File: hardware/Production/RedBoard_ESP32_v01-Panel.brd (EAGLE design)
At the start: 246.1 x 248.9 mm, 2454 parts, among them J1 5.5x2.1mm Barrel, J101 USB C, J102 USB_SOLDER_PADS, J103 M10NO_SILK, J108 QWIIC_RIGHT_ANGLE, J109 MICRO-SD-PUSH-PUSH-EXT-PIN, J110 5.5x2.1mm Barrel, J117 USB C, J118 USB_SOLDER_PADS, J119 M10NO_SILK, J124 QWIIC_RIGHT_ANGLE, J125 MICRO-SD-PUSH-PUSH-EXT-PIN, J126 5.5x2.1mm Barrel, J13 QWIIC_RIGHT_ANGLE, J133 USB C, J134 USB_SOLDER_PADS, J135 M10NO_SILK, J140 QWIIC_RIGHT_ANGLE, J141 MICRO-SD-PUSH-PUSH-EXT-PIN, J142 5.5x2.1mm Barrel, J149 USB C, J15 MICRO-SD-PUSH-PUSH-EXT-PIN, J150 USB_SOLDER_PADS, J151 M10NO_SILK, J156 QWIIC_RIGHT_ANGLE, J157 MICRO-SD-PUSH-PUSH-EXT-PIN, J158 5.5x2.1mm Barrel, J165 USB C, J166 USB_SOLDER_PADS, J167 M10NO_SILK, J172 QWIIC_RIGHT_ANGLE, J173 MICRO-SD-PUSH-PUSH-EXT-PIN, J174 5.5x2.1mm Barrel, J181 USB C, J182 USB_SOLDER_PADS, J183 M10NO_SILK, J188 QWIIC_RIGHT_ANGLE, J189 MICRO-SD-PUSH-PUSH-EXT-PIN, J190 5.5x2.1mm Barrel, J2 USB C, J21 USB C, J22 USB_SOLDER_PADS, J23 M10NO_SILK, J28 QWIIC_RIGHT_ANGLE, J29 MICRO-SD-PUSH-PUSH-EXT-PIN, J3 USB_SOLDER_PADS, J30 5.5x2.1mm Barrel, J37 USB C, J38 USB_SOLDER_PADS, J39 M10NO_SILK, J44 QWIIC_RIGHT_ANGLE, J45 MICRO-SD-PUSH-PUSH-EXT-PIN, J46 5.5x2.1mm Barrel, J5 M10NO_SILK, J53 USB C, J54 USB_SOLDER_PADS, J55 M10NO_SILK, J60 QWIIC_RIGHT_ANGLE, J61 MICRO-SD-PUSH-PUSH-EXT-PIN, J62 5.5x2.1mm Barrel, J69 USB C, J70 USB_SOLDER_PADS, J71 M10NO_SILK, J76 QWIIC_RIGHT_ANGLE, J77 MICRO-SD-PUSH-PUSH-EXT-PIN, J78 5.5x2.1mm Barrel, J85 USB C, J86 USB_SOLDER_PADS, J87 M10NO_SILK, J92 QWIIC_RIGHT_ANGLE, J93 MICRO-SD-PUSH-PUSH-EXT-PIN, J94 5.5x2.1mm Barrel, Q1 MBT3904DW1T1, Q100 20V/4.2A/52mΩ/1.4W, Q102 20V/4.2A/52mΩ/1.4W, Q104 20V/4.2A/52mΩ/1.4W, Q105 MBT3904DW1T1, Q107 20V/4.2A/52mΩ/1.4W, Q109 20V/4.2A/52mΩ/1.4W, Q11 20V/4.2A/52mΩ/1.4W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

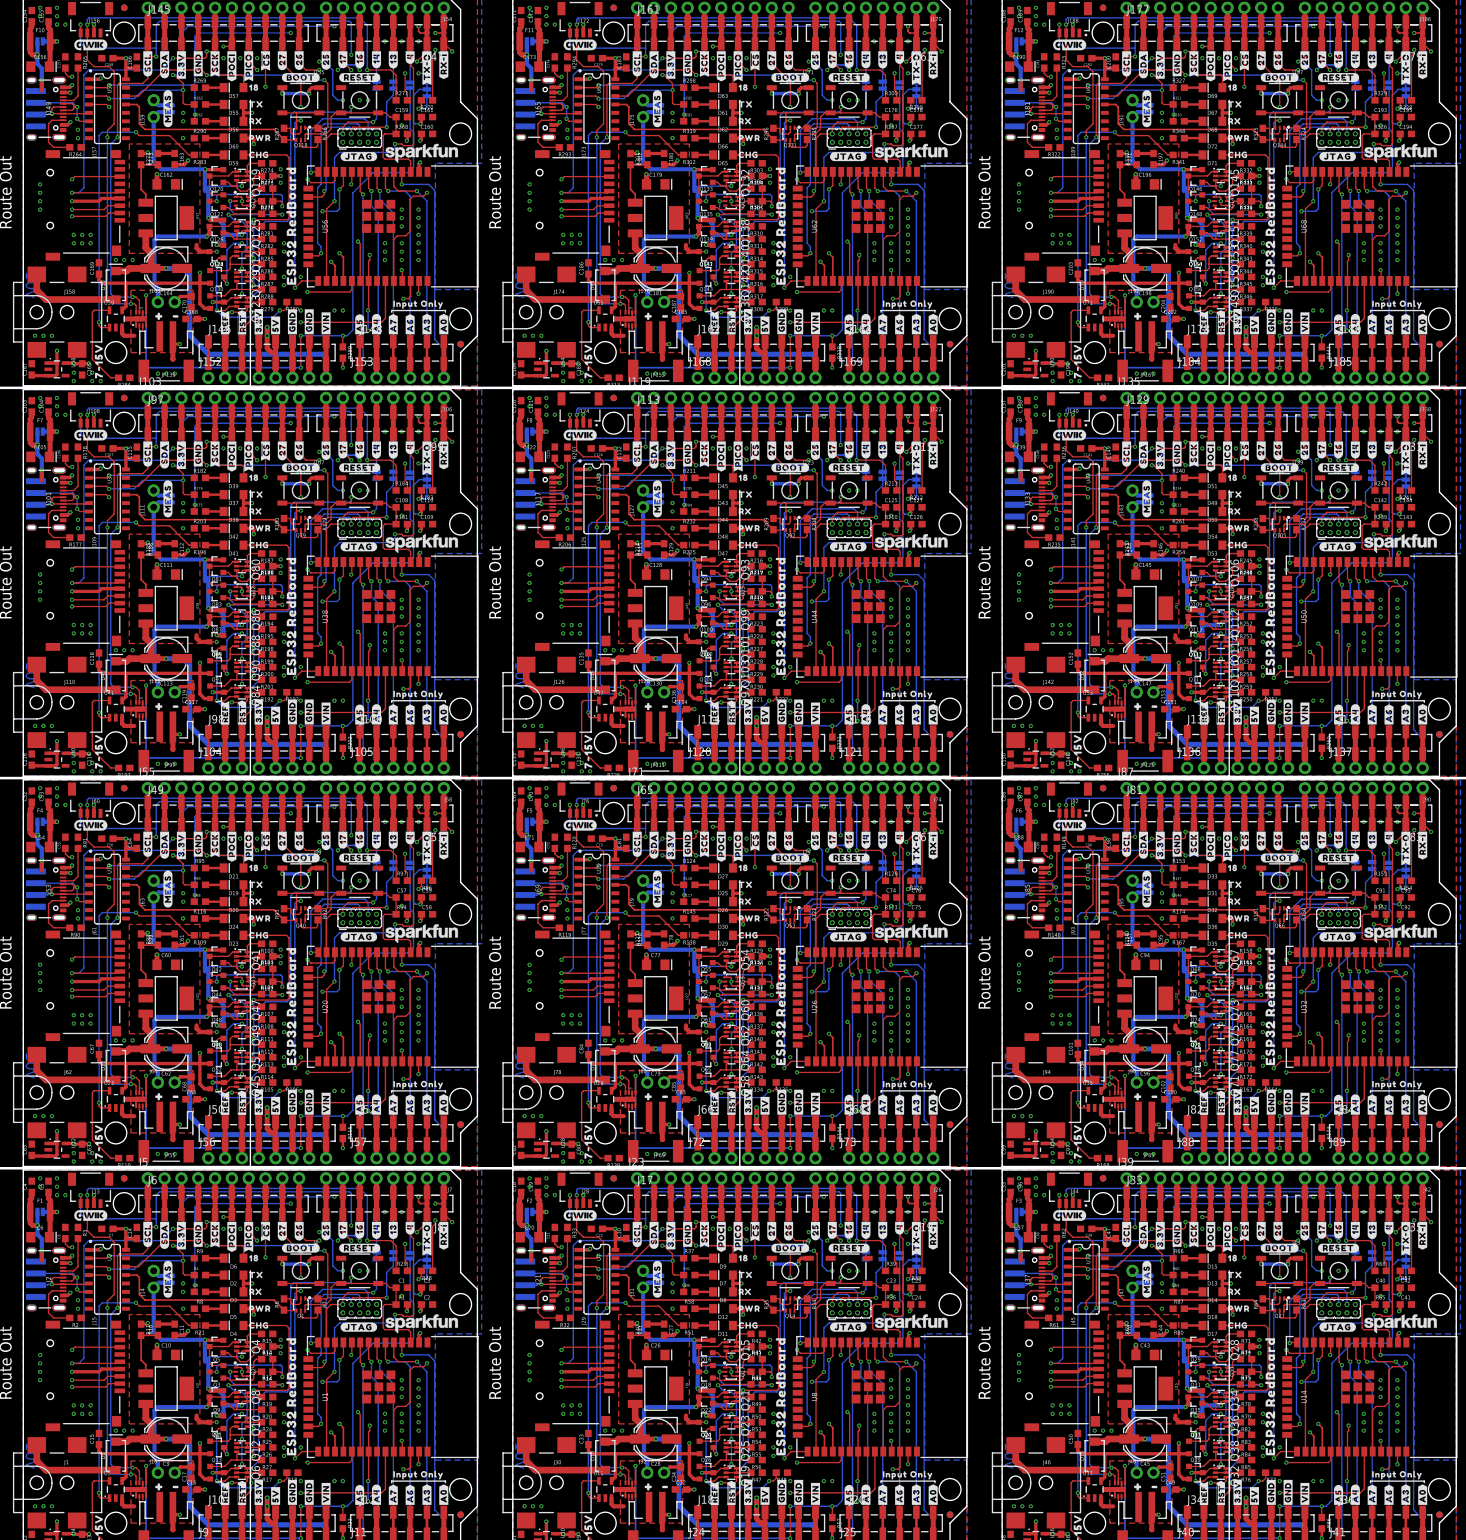
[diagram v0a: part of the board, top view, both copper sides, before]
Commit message: Added Test Point per Eric Orosel request.
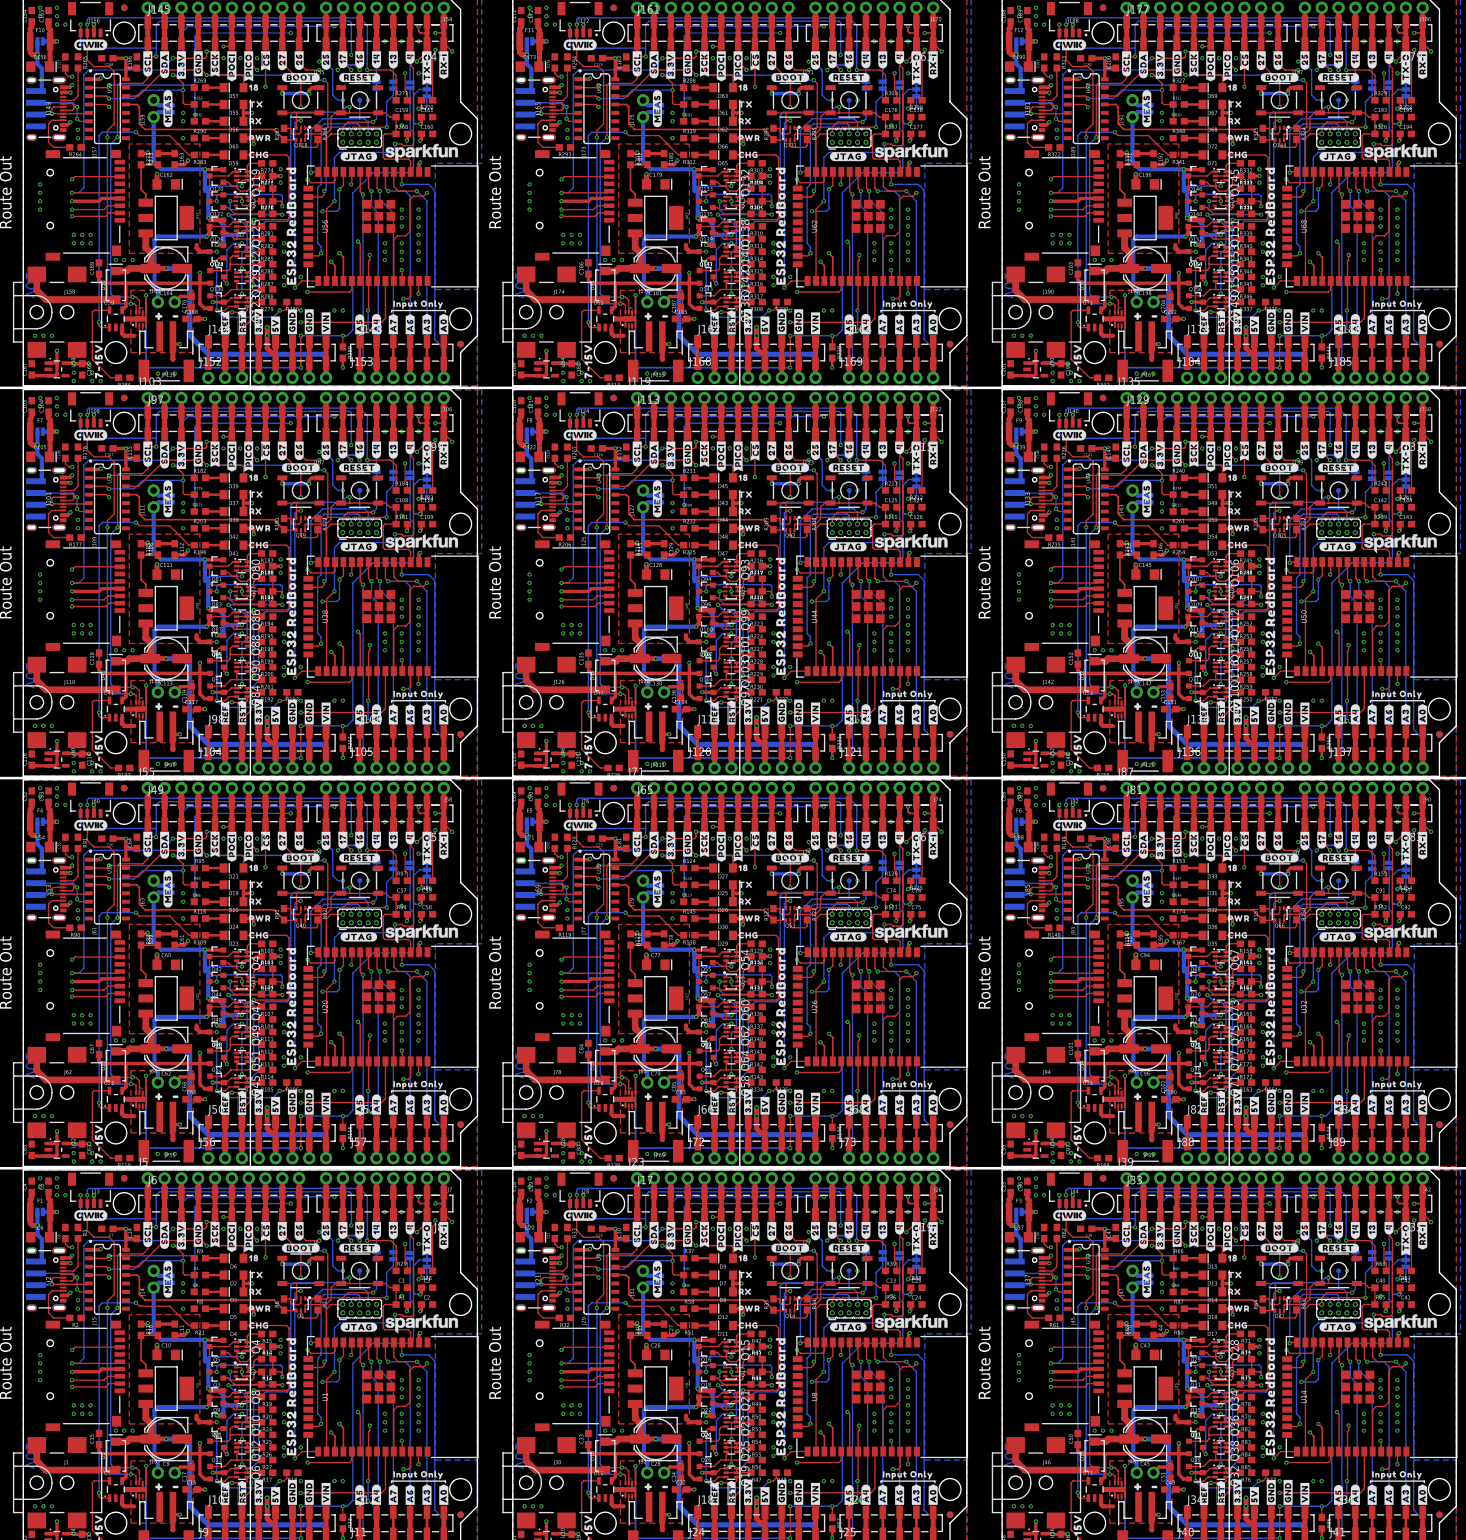
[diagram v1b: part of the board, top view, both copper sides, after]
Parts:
- added TP1, TP10, TP11, TP12, TP2, TP3, TP4, TP5, TP6, TP7, TP8, TP9: TEST-POINT3, SparkFun-Connectors:PAD.03X.03
- added U$1129: (no value), output-ESP32:#1850
- added U$1130: (no value), output-ESP32:#I2C#1855
- added U$1131: (no value), output-ESP32:##ALERT##1852
- added U$1132: (no value), output-ESP32:#TMS#1854
- added U$1133: (no value), output-ESP32:#TCK#1853
- added U$1134: (no value), output-ESP32:MADE_IN_THE_USA321857
- added U$1135: (no value), output-ESP32:ESP32_REDBOARD321857
- added U$1136: (no value), output-ESP32:REDBOARD321856
- added U$1137, U$1138: (no value), output-ESP32:INPUT_ONLY321867
- added U$1139: (no value), output-ESP32:##ALERT##4#321866
- added U$1140: (no value), output-ESP32:TP1321868
- U$100: device output-ESP32:#SCK#31 -> output-ESP32:#GND#32
- U$1000: device output-ESP32:#IOREF#321865 -> output-ESP32:#34#A6#32321865
- U$1001: device output-ESP32:#3#RX#I#32321869 -> output-ESP32:#35#A7#321862
- U$1002: device output-ESP32:#1#TX#O#32321869 -> output-ESP32:#32#A4#32321865
- U$1003: device output-ESP32:#13#TCK#32321869 -> output-ESP32:#34#A6#321862
- U$1004: device output-ESP32:#14#TMS#32321869 -> output-ESP32:#VIN#321862
- U$1005, U$723: device output-ESP32:#16#32321869 -> output-ESP32:#GND#321863
- U$1006: device output-ESP32:#17#32321869 -> output-ESP32:#5V#321864
- U$1007: device output-ESP32:#25#32321869 -> output-ESP32:#3#3V#321864
- U$1008: device output-ESP32:#26#32321869 -> output-ESP32:#GND#321863
- U$1009: device output-ESP32:#5##CS##32321869 -> output-ESP32:##RESET##321864
- U$101: device output-ESP32:#POCI#30 -> output-ESP32:#SCK#31
- U$1010: device output-ESP32:#23#PICO#321866 -> output-ESP32:#IOREF#321865
- U$1011: device output-ESP32:#19#POCI#321866 -> output-ESP32:#3#RX#I#32321869
- U$1012: device output-ESP32:#18#SCK#32321869 -> output-ESP32:#1#TX#O#32321869
- U$1013: device output-ESP32:#21#SDA#32321869 -> output-ESP32:#13#TCK#32321869
- U$1014: device output-ESP32:#22#SCL#32321869 -> output-ESP32:#14#TMS#32321869
- U$1015: device output-ESP32:#27#32321869 -> output-ESP32:#16#32321869
- U$1016: device output-ESP32:#GND#321866 -> output-ESP32:#17#32321869
- U$1017: device output-ESP32:#3#3V#321866 -> output-ESP32:#25#32321869
- U$1018: device output-ESP32:#MEAS#1851 -> output-ESP32:#26#32321869
- U$1019: device output-ESP32:#BYP#35 -> output-ESP32:#5##CS##32321869
- U$102: device output-ESP32:#PICO#29 -> output-ESP32:#POCI#30
- U$1020: device output-ESP32:D#32321863 -> output-ESP32:#23#PICO#321866
- U$1021: device output-ESP32:D#32321862 -> output-ESP32:#19#POCI#321866
- U$1022: device output-ESP32:G32321864 -> output-ESP32:#18#SCK#32321869
- U$1023: device output-ESP32:#1849 -> output-ESP32:#21#SDA#32321869
- U$1024: device output-ESP32:#1850 -> output-ESP32:#22#SCL#32321869
- U$1025: device output-ESP32:#I2C#1855 -> output-ESP32:#27#32321869
- U$1026: device output-ESP32:##ALERT##1852 -> output-ESP32:#GND#321866
- U$1027: device output-ESP32:#TMS#1854 -> output-ESP32:#3#3V#321866
- U$1028: device output-ESP32:#TCK#1853 -> output-ESP32:#MEAS#1851
- U$1029: device output-ESP32:MADE_IN_THE_USA321857 -> output-ESP32:#BYP#35
- U$103: device output-ESP32:1836 -> output-ESP32:#PICO#29
- U$1030: device output-ESP32:ESP32_REDBOARD321857 -> output-ESP32:D#32321863
- U$1031: device output-ESP32:REDBOARD321856 -> output-ESP32:D#32321862
- U$1032, U$1127: device output-ESP32:INPUT_ONLY321867 -> output-ESP32:G32321864
- U$1033, U$938: device output-ESP32:INPUT_ONLY321867 -> output-ESP32:#1849
- U$1034: device output-ESP32:##ALERT##4#321866 -> output-ESP32:#1850
- U$1035: device output-ESP32:V323252 -> output-ESP32:#I2C#1855
- U$1036: device output-ESP32:#SCL#34 -> output-ESP32:##ALERT##1852
- U$1037: device output-ESP32:#SDA#33 -> output-ESP32:#TMS#1854
- U$1038: device output-ESP32:#3#3V#33 -> output-ESP32:#TCK#1853
- U$1039: device output-ESP32:#GND#32 -> output-ESP32:MADE_IN_THE_USA321857
- U$104: device output-ESP32:##CS##28 -> output-ESP32:1836
- U$1040: device output-ESP32:#SCK#31 -> output-ESP32:ESP32_REDBOARD321857
- U$1041: device output-ESP32:#POCI#30 -> output-ESP32:REDBOARD321856
- U$1042, U$948: device output-ESP32:#PICO#29 -> output-ESP32:INPUT_ONLY321867
- U$1043: device output-ESP32:1836 -> output-ESP32:INPUT_ONLY321867
- U$1044: device output-ESP32:##CS##28 -> output-ESP32:##ALERT##4#321866
- U$1045: device output-ESP32:#27#27 -> output-ESP32:TP1321868
- U$1046: device output-ESP32:#26#26 -> output-ESP32:V323252
- U$1047: device output-ESP32:TX1838 -> output-ESP32:#SCL#34
- U$1048: device output-ESP32:RX1839 -> output-ESP32:#SDA#33
- U$1049: device output-ESP32:PWR1837 -> output-ESP32:#3#3V#33
- U$105: device output-ESP32:#27#27 -> output-ESP32:##CS##28
- U$1050: device output-ESP32:CHG1840 -> output-ESP32:#GND#32
- U$1051: device output-ESP32:#25#18 -> output-ESP32:#SCK#31
- U$1052: device output-ESP32:#17#17 -> output-ESP32:#POCI#30
- U$1053: device output-ESP32:#16#15 -> output-ESP32:#PICO#29
- U$1054: device output-ESP32:#14#14 -> output-ESP32:1836
- U$1055: device output-ESP32:#13#5 -> output-ESP32:##CS##28
- U$1056: device output-ESP32:#4#2 -> output-ESP32:#27#27
- U$1057: device output-ESP32:#TX#O#0 -> output-ESP32:#26#26
- U$1058: device output-ESP32:#RX#I#1 -> output-ESP32:TX1838
- U$1059: device output-ESP32:#RESET#1842 -> output-ESP32:RX1839
- U$106: device output-ESP32:#26#26 -> output-ESP32:#27#27
- U$1060: device output-ESP32:#BOOT#1841 -> output-ESP32:PWR1837
- U$1061: device output-ESP32:#JTAG#1847 -> output-ESP32:CHG1840
- U$1062: device output-ESP32:#A0#1843 -> output-ESP32:#25#18
- U$1063: device output-ESP32:#A3#1843 -> output-ESP32:#17#17
- U$1064: device output-ESP32:#A6#1843 -> output-ESP32:#16#15
- U$1065: device output-ESP32:#A7#1843 -> output-ESP32:#14#14
- U$1066: device output-ESP32:#A4#1843 -> output-ESP32:#13#5
- U$1067: device output-ESP32:#A5#1843 -> output-ESP32:#4#2
- U$1068: device output-ESP32:#VIN#1843 -> output-ESP32:#TX#O#0
- U$1069: device output-ESP32:#GND#1844 -> output-ESP32:#RX#I#1
- U$107: device output-ESP32:TX1838 -> output-ESP32:#26#26
- U$1070, U$975: device output-ESP32:#GND#1844 -> output-ESP32:#RESET#1842
- U$1071: device output-ESP32:#5V#1845 -> output-ESP32:#BOOT#1841
- U$1072: device output-ESP32:#3#3V#1845 -> output-ESP32:#JTAG#1847
- U$1073: device output-ESP32:##RST##1845 -> output-ESP32:#A0#1843
- U$1074: device output-ESP32:#REF#1846 -> output-ESP32:#A3#1843
- U$1075: device output-ESP32:#MEAS#1851 -> output-ESP32:#A6#1843
- U$1076: device output-ESP32:#1849 -> output-ESP32:#A7#1843
- U$1077: device output-ESP32:#1850 -> output-ESP32:#A4#1843
- U$1078: device output-ESP32:#BATT#1848 -> output-ESP32:#A5#1843
- U$1079: device output-ESP32:#JTAG#1847 -> output-ESP32:#VIN#1843
- U$108: device output-ESP32:RX1839 -> output-ESP32:TX1838
- U$1080, U$986: device output-ESP32:ESP321855 -> output-ESP32:#GND#1844
- U$1081: device output-ESP32:7#15V32321861 -> output-ESP32:#GND#1844
- U$1082: device output-ESP32:#39#A3#321862 -> output-ESP32:#5V#1845
- U$1083: device output-ESP32:#36#A0#321862 -> output-ESP32:#3#3V#1845
- U$1084: device output-ESP32:#34#A6#32321865 -> output-ESP32:##RST##1845
- U$1085: device output-ESP32:#35#A7#321862 -> output-ESP32:#REF#1846
- U$1086: device output-ESP32:#32#A4#32321865 -> output-ESP32:#MEAS#1851
- U$1087: device output-ESP32:#34#A6#321862 -> output-ESP32:#1849
- U$1088: device output-ESP32:#VIN#321862 -> output-ESP32:#1850
- U$1089: device output-ESP32:#GND#321863 -> output-ESP32:#BATT#1848
- U$109: device output-ESP32:PWR1837 -> output-ESP32:RX1839
- U$1090: device output-ESP32:#5V#321864 -> output-ESP32:#JTAG#1847
- U$1091: device output-ESP32:#3#3V#321864 -> output-ESP32:ESP321855
- U$1092, U$807: device output-ESP32:#GND#321863 -> output-ESP32:7#15V32321861
- U$1093: device output-ESP32:##RESET##321864 -> output-ESP32:#39#A3#321862
- U$1094: device output-ESP32:#IOREF#321865 -> output-ESP32:#36#A0#321862
- U$1095: device output-ESP32:#3#RX#I#32321869 -> output-ESP32:#34#A6#32321865
- U$1096: device output-ESP32:#1#TX#O#32321869 -> output-ESP32:#35#A7#321862
- U$1097: device output-ESP32:#13#TCK#32321869 -> output-ESP32:#32#A4#32321865
- U$1098: device output-ESP32:#14#TMS#32321869 -> output-ESP32:#34#A6#321862
- U$1099: device output-ESP32:#16#32321869 -> output-ESP32:#VIN#321862
- U$110: device output-ESP32:CHG1840 -> output-ESP32:PWR1837
- U$1100, U$818: device output-ESP32:#17#32321869 -> output-ESP32:#GND#321863
- U$1101: device output-ESP32:#25#32321869 -> output-ESP32:#5V#321864
- U$1102: device output-ESP32:#26#32321869 -> output-ESP32:#3#3V#321864
- U$1103: device output-ESP32:#5##CS##32321869 -> output-ESP32:#GND#321863
- U$1104: device output-ESP32:#23#PICO#321866 -> output-ESP32:##RESET##321864
- U$1105: device output-ESP32:#19#POCI#321866 -> output-ESP32:#IOREF#321865
- U$1106: device output-ESP32:#18#SCK#32321869 -> output-ESP32:#3#RX#I#32321869
- U$1107: device output-ESP32:#21#SDA#32321869 -> output-ESP32:#1#TX#O#32321869
- U$1108: device output-ESP32:#22#SCL#32321869 -> output-ESP32:#13#TCK#32321869
- U$1109: device output-ESP32:#27#32321869 -> output-ESP32:#14#TMS#32321869
- U$111: device output-ESP32:#25#18 -> output-ESP32:CHG1840
- U$1110: device output-ESP32:#GND#321866 -> output-ESP32:#16#32321869
- U$1111: device output-ESP32:#3#3V#321866 -> output-ESP32:#17#32321869
- U$1112: device output-ESP32:#MEAS#1851 -> output-ESP32:#25#32321869
- U$1113: device output-ESP32:#BYP#35 -> output-ESP32:#26#32321869
- U$1114: device output-ESP32:D#32321863 -> output-ESP32:#5##CS##32321869
- U$1115: device output-ESP32:D#32321862 -> output-ESP32:#23#PICO#321866
- U$1116: device output-ESP32:G32321864 -> output-ESP32:#19#POCI#321866
- U$1117: device output-ESP32:#1849 -> output-ESP32:#18#SCK#32321869
- U$1118: device output-ESP32:#1850 -> output-ESP32:#21#SDA#32321869
- U$1119: device output-ESP32:#I2C#1855 -> output-ESP32:#22#SCL#32321869
- U$112: device output-ESP32:#17#17 -> output-ESP32:#25#18
- U$1120: device output-ESP32:##ALERT##1852 -> output-ESP32:#27#32321869
- U$1121: device output-ESP32:#TMS#1854 -> output-ESP32:#GND#321866
- U$1122: device output-ESP32:#TCK#1853 -> output-ESP32:#3#3V#321866
- U$1123: device output-ESP32:MADE_IN_THE_USA321857 -> output-ESP32:#MEAS#1851
- U$1124: device output-ESP32:ESP32_REDBOARD321857 -> output-ESP32:#BYP#35
- U$1125: device output-ESP32:REDBOARD321856 -> output-ESP32:D#32321863
- U$1126: device output-ESP32:INPUT_ONLY321867 -> output-ESP32:D#32321862
- U$1128: device output-ESP32:##ALERT##4#321866 -> output-ESP32:#1849
- U$113: device output-ESP32:#16#15 -> output-ESP32:#17#17
- U$114: device output-ESP32:#14#14 -> output-ESP32:#16#15
- U$115: device output-ESP32:#13#5 -> output-ESP32:#14#14
- U$116: device output-ESP32:#4#2 -> output-ESP32:#13#5
- U$117: device output-ESP32:#TX#O#0 -> output-ESP32:#4#2
- U$118: device output-ESP32:#RX#I#1 -> output-ESP32:#TX#O#0
- U$119: device output-ESP32:#RESET#1842 -> output-ESP32:#RX#I#1
- U$120: device output-ESP32:#BOOT#1841 -> output-ESP32:#RESET#1842
- U$121: device output-ESP32:#JTAG#1847 -> output-ESP32:#BOOT#1841
- U$122: device output-ESP32:#A0#1843 -> output-ESP32:#JTAG#1847
- U$123: device output-ESP32:#A3#1843 -> output-ESP32:#A0#1843
- U$124: device output-ESP32:#A6#1843 -> output-ESP32:#A3#1843
- U$125: device output-ESP32:#A7#1843 -> output-ESP32:#A6#1843
- U$126: device output-ESP32:#A4#1843 -> output-ESP32:#A7#1843
- U$127: device output-ESP32:#A5#1843 -> output-ESP32:#A4#1843
- U$128: device output-ESP32:#VIN#1843 -> output-ESP32:#A5#1843
- U$129, U$224: device output-ESP32:#GND#1844 -> output-ESP32:#VIN#1843
- U$131, U$225: device output-ESP32:#5V#1845 -> output-ESP32:#GND#1844
- U$132: device output-ESP32:#3#3V#1845 -> output-ESP32:#5V#1845
- U$133: device output-ESP32:##RST##1845 -> output-ESP32:#3#3V#1845
- U$134: device output-ESP32:#REF#1846 -> output-ESP32:##RST##1845
- U$135: device output-ESP32:#MEAS#1851 -> output-ESP32:#REF#1846
- U$136, U$553: device output-ESP32:#1849 -> output-ESP32:#MEAS#1851
- U$137, U$178: device output-ESP32:#1850 -> output-ESP32:#1849
- U$138: device output-ESP32:#BATT#1848 -> output-ESP32:#1850
- U$139: device output-ESP32:#JTAG#1847 -> output-ESP32:#BATT#1848
- U$140: device output-ESP32:ESP321855 -> output-ESP32:#JTAG#1847
- U$141: device output-ESP32:7#15V32321861 -> output-ESP32:ESP321855
- U$142: device output-ESP32:#39#A3#321862 -> output-ESP32:7#15V32321861
- U$143: device output-ESP32:#36#A0#321862 -> output-ESP32:#39#A3#321862
- U$144: device output-ESP32:#34#A6#32321865 -> output-ESP32:#36#A0#321862
- U$145: device output-ESP32:#35#A7#321862 -> output-ESP32:#34#A6#32321865
- U$146: device output-ESP32:#32#A4#32321865 -> output-ESP32:#35#A7#321862
- U$147: device output-ESP32:#34#A6#321862 -> output-ESP32:#32#A4#32321865
- U$148: device output-ESP32:#VIN#321862 -> output-ESP32:#34#A6#321862
- U$149, U$434: device output-ESP32:#GND#321863 -> output-ESP32:#VIN#321862
- U$150: device output-ESP32:#5V#321864 -> output-ESP32:#GND#321863
- U$151: device output-ESP32:#3#3V#321864 -> output-ESP32:#5V#321864
- U$152: device output-ESP32:#GND#321863 -> output-ESP32:#3#3V#321864
- U$153, U$435: device output-ESP32:##RESET##321864 -> output-ESP32:#GND#321863
- U$154: device output-ESP32:#IOREF#321865 -> output-ESP32:##RESET##321864
- U$155: device output-ESP32:#3#RX#I#32321869 -> output-ESP32:#IOREF#321865
- U$156: device output-ESP32:#1#TX#O#32321869 -> output-ESP32:#3#RX#I#32321869
- U$157: device output-ESP32:#13#TCK#32321869 -> output-ESP32:#1#TX#O#32321869
- U$158: device output-ESP32:#14#TMS#32321869 -> output-ESP32:#13#TCK#32321869
- U$159: device output-ESP32:#16#32321869 -> output-ESP32:#14#TMS#32321869
- U$160: device output-ESP32:#17#32321869 -> output-ESP32:#16#32321869
- U$161: device output-ESP32:#25#32321869 -> output-ESP32:#17#32321869
- U$162: device output-ESP32:#26#32321869 -> output-ESP32:#25#32321869
- U$163: device output-ESP32:#5##CS##32321869 -> output-ESP32:#26#32321869
- U$164: device output-ESP32:#23#PICO#321866 -> output-ESP32:#5##CS##32321869
- U$165: device output-ESP32:#19#POCI#321866 -> output-ESP32:#23#PICO#321866
- U$166: device output-ESP32:#18#SCK#32321869 -> output-ESP32:#19#POCI#321866
- U$167: device output-ESP32:#21#SDA#32321869 -> output-ESP32:#18#SCK#32321869
- U$168: device output-ESP32:#22#SCL#32321869 -> output-ESP32:#21#SDA#32321869
- U$169: device output-ESP32:#27#32321869 -> output-ESP32:#22#SCL#32321869
- U$170: device output-ESP32:#GND#321866 -> output-ESP32:#27#32321869
- U$171: device output-ESP32:#3#3V#321866 -> output-ESP32:#GND#321866
- U$172: device output-ESP32:#MEAS#1851 -> output-ESP32:#3#3V#321866
- U$173: device output-ESP32:#BYP#35 -> output-ESP32:#MEAS#1851
- U$174: device output-ESP32:D#32321863 -> output-ESP32:#BYP#35
- U$175: device output-ESP32:D#32321862 -> output-ESP32:D#32321863
- U$176: device output-ESP32:G32321864 -> output-ESP32:D#32321862
- U$177: device output-ESP32:#1849 -> output-ESP32:G32321864
- U$179: device output-ESP32:#I2C#1855 -> output-ESP32:#1850
- U$180: device output-ESP32:##ALERT##1852 -> output-ESP32:#I2C#1855
- U$181: device output-ESP32:#TMS#1854 -> output-ESP32:##ALERT##1852
- U$182: device output-ESP32:#TCK#1853 -> output-ESP32:#TMS#1854
- U$183: device output-ESP32:MADE_IN_THE_USA321857 -> output-ESP32:#TCK#1853
- U$184: device output-ESP32:ESP32_REDBOARD321857 -> output-ESP32:MADE_IN_THE_USA321857
- U$185: device output-ESP32:REDBOARD321856 -> output-ESP32:ESP32_REDBOARD321857
- U$186, U$281: device output-ESP32:INPUT_ONLY321867 -> output-ESP32:REDBOARD321856
- U$188, U$282: device output-ESP32:##ALERT##4#321866 -> output-ESP32:INPUT_ONLY321867
- U$189: device output-ESP32:V323252 -> output-ESP32:##ALERT##4#321866
- U$190: device output-ESP32:#SCL#34 -> output-ESP32:TP1321868
- U$191: device output-ESP32:#SDA#33 -> output-ESP32:V323252
- U$192: device output-ESP32:#3#3V#33 -> output-ESP32:#SCL#34
- U$193: device output-ESP32:#GND#32 -> output-ESP32:#SDA#33
- U$194: device output-ESP32:#SCK#31 -> output-ESP32:#3#3V#33
- U$195: device output-ESP32:#POCI#30 -> output-ESP32:#GND#32
- U$196: device output-ESP32:#PICO#29 -> output-ESP32:#SCK#31
- U$197: device output-ESP32:1836 -> output-ESP32:#POCI#30
- U$198: device output-ESP32:##CS##28 -> output-ESP32:#PICO#29
- U$199: device output-ESP32:#27#27 -> output-ESP32:1836
- U$200: device output-ESP32:#26#26 -> output-ESP32:##CS##28
- U$201: device output-ESP32:TX1838 -> output-ESP32:#27#27
- U$202: device output-ESP32:RX1839 -> output-ESP32:#26#26
- U$203: device output-ESP32:PWR1837 -> output-ESP32:TX1838
- U$204: device output-ESP32:CHG1840 -> output-ESP32:RX1839
- U$205: device output-ESP32:#25#18 -> output-ESP32:PWR1837
- U$206: device output-ESP32:#17#17 -> output-ESP32:CHG1840
- U$207: device output-ESP32:#16#15 -> output-ESP32:#25#18
- U$208: device output-ESP32:#14#14 -> output-ESP32:#17#17
- U$209: device output-ESP32:#13#5 -> output-ESP32:#16#15
- U$210: device output-ESP32:#4#2 -> output-ESP32:#14#14
- U$211: device output-ESP32:#TX#O#0 -> output-ESP32:#13#5
- U$212: device output-ESP32:#RX#I#1 -> output-ESP32:#4#2
- U$213: device output-ESP32:#RESET#1842 -> output-ESP32:#TX#O#0
- U$214: device output-ESP32:#BOOT#1841 -> output-ESP32:#RX#I#1
- U$215: device output-ESP32:#JTAG#1847 -> output-ESP32:#RESET#1842
- U$216: device output-ESP32:#A0#1843 -> output-ESP32:#BOOT#1841
- U$217: device output-ESP32:#A3#1843 -> output-ESP32:#JTAG#1847
- U$218: device output-ESP32:#A6#1843 -> output-ESP32:#A0#1843
- U$219: device output-ESP32:#A7#1843 -> output-ESP32:#A3#1843
- U$220: device output-ESP32:#A4#1843 -> output-ESP32:#A6#1843
- U$221: device output-ESP32:#A5#1843 -> output-ESP32:#A7#1843
- U$222: device output-ESP32:#VIN#1843 -> output-ESP32:#A4#1843
- U$223, U$318: device output-ESP32:#GND#1844 -> output-ESP32:#A5#1843
- U$226, U$320: device output-ESP32:#3#3V#1845 -> output-ESP32:#GND#1844
- U$227: device output-ESP32:##RST##1845 -> output-ESP32:#5V#1845
- U$228: device output-ESP32:#REF#1846 -> output-ESP32:#3#3V#1845
- U$229: device output-ESP32:#MEAS#1851 -> output-ESP32:##RST##1845
- U$230: device output-ESP32:#1849 -> output-ESP32:#REF#1846
- U$231, U$648: device output-ESP32:#1850 -> output-ESP32:#MEAS#1851
- U$232: device output-ESP32:#BATT#1848 -> output-ESP32:#1849
- U$233: device output-ESP32:#JTAG#1847 -> output-ESP32:#1850
- U$234: device output-ESP32:ESP321855 -> output-ESP32:#BATT#1848
- U$235: device output-ESP32:7#15V32321861 -> output-ESP32:#JTAG#1847
- U$236: device output-ESP32:#39#A3#321862 -> output-ESP32:ESP321855
- U$237: device output-ESP32:#36#A0#321862 -> output-ESP32:7#15V32321861
- U$238: device output-ESP32:#34#A6#32321865 -> output-ESP32:#39#A3#321862
- U$239: device output-ESP32:#35#A7#321862 -> output-ESP32:#36#A0#321862
- U$240: device output-ESP32:#32#A4#32321865 -> output-ESP32:#34#A6#32321865
- U$241: device output-ESP32:#34#A6#321862 -> output-ESP32:#35#A7#321862
- U$242: device output-ESP32:#VIN#321862 -> output-ESP32:#32#A4#32321865
- U$243, U$528: device output-ESP32:#GND#321863 -> output-ESP32:#34#A6#321862
- U$244: device output-ESP32:#5V#321864 -> output-ESP32:#VIN#321862
- U$245: device output-ESP32:#3#3V#321864 -> output-ESP32:#GND#321863
- U$246: device output-ESP32:#GND#321863 -> output-ESP32:#5V#321864
- U$247: device output-ESP32:##RESET##321864 -> output-ESP32:#3#3V#321864
- U$248, U$530: device output-ESP32:#IOREF#321865 -> output-ESP32:#GND#321863
- U$249: device output-ESP32:#3#RX#I#32321869 -> output-ESP32:##RESET##321864
- U$250: device output-ESP32:#1#TX#O#32321869 -> output-ESP32:#IOREF#321865
- U$251: device output-ESP32:#13#TCK#32321869 -> output-ESP32:#3#RX#I#32321869
- U$252: device output-ESP32:#14#TMS#32321869 -> output-ESP32:#1#TX#O#32321869
- U$253: device output-ESP32:#16#32321869 -> output-ESP32:#13#TCK#32321869
- U$254: device output-ESP32:#17#32321869 -> output-ESP32:#14#TMS#32321869
- U$255: device output-ESP32:#25#32321869 -> output-ESP32:#16#32321869
- U$256: device output-ESP32:#26#32321869 -> output-ESP32:#17#32321869
- U$257: device output-ESP32:#5##CS##32321869 -> output-ESP32:#25#32321869
- U$258: device output-ESP32:#23#PICO#321866 -> output-ESP32:#26#32321869
- U$259: device output-ESP32:#19#POCI#321866 -> output-ESP32:#5##CS##32321869
- U$260: device output-ESP32:#18#SCK#32321869 -> output-ESP32:#23#PICO#321866
- U$261: device output-ESP32:#21#SDA#32321869 -> output-ESP32:#19#POCI#321866
- U$262: device output-ESP32:#22#SCL#32321869 -> output-ESP32:#18#SCK#32321869
- U$263: device output-ESP32:#27#32321869 -> output-ESP32:#21#SDA#32321869
- U$264: device output-ESP32:#GND#321866 -> output-ESP32:#22#SCL#32321869
- U$265: device output-ESP32:#3#3V#321866 -> output-ESP32:#27#32321869
- U$266: device output-ESP32:#MEAS#1851 -> output-ESP32:#GND#321866
- U$267: device output-ESP32:#BYP#35 -> output-ESP32:#3#3V#321866
- U$268: device output-ESP32:D#32321863 -> output-ESP32:#MEAS#1851
- U$269: device output-ESP32:D#32321862 -> output-ESP32:#BYP#35
- U$270: device output-ESP32:G32321864 -> output-ESP32:D#32321863
- U$271: device output-ESP32:#1849 -> output-ESP32:D#32321862
- U$272: device output-ESP32:#1850 -> output-ESP32:G32321864
- U$273: device output-ESP32:#I2C#1855 -> output-ESP32:#1849
- U$274: device output-ESP32:##ALERT##1852 -> output-ESP32:#1850
- U$275: device output-ESP32:#TMS#1854 -> output-ESP32:#I2C#1855
- U$276: device output-ESP32:#TCK#1853 -> output-ESP32:##ALERT##1852
- U$277: device output-ESP32:MADE_IN_THE_USA321857 -> output-ESP32:#TMS#1854
- U$278: device output-ESP32:ESP32_REDBOARD321857 -> output-ESP32:#TCK#1853
- U$279: device output-ESP32:REDBOARD321856 -> output-ESP32:MADE_IN_THE_USA321857
- U$280, U$375: device output-ESP32:INPUT_ONLY321867 -> output-ESP32:ESP32_REDBOARD321857
- U$283, U$377: device output-ESP32:V323252 -> output-ESP32:INPUT_ONLY321867
- U$284: device output-ESP32:#SCL#34 -> output-ESP32:##ALERT##4#321866
- U$285, U$95: device output-ESP32:#SDA#33 -> output-ESP32:TP1321868
- U$286: device output-ESP32:#3#3V#33 -> output-ESP32:V323252
- U$287: device output-ESP32:#GND#32 -> output-ESP32:#SCL#34
- U$288: device output-ESP32:#SCK#31 -> output-ESP32:#SDA#33
- U$289: device output-ESP32:#POCI#30 -> output-ESP32:#3#3V#33
- U$290: device output-ESP32:#PICO#29 -> output-ESP32:#GND#32
- U$291: device output-ESP32:1836 -> output-ESP32:#SCK#31
- U$292: device output-ESP32:##CS##28 -> output-ESP32:#POCI#30
- U$293: device output-ESP32:#27#27 -> output-ESP32:#PICO#29
- U$294: device output-ESP32:#26#26 -> output-ESP32:1836
- U$295: device output-ESP32:TX1838 -> output-ESP32:##CS##28
- U$296: device output-ESP32:RX1839 -> output-ESP32:#27#27
- U$297: device output-ESP32:PWR1837 -> output-ESP32:#26#26
- U$298: device output-ESP32:CHG1840 -> output-ESP32:TX1838
- U$299: device output-ESP32:#25#18 -> output-ESP32:RX1839
- U$300: device output-ESP32:#17#17 -> output-ESP32:PWR1837
- U$301: device output-ESP32:#16#15 -> output-ESP32:CHG1840
- U$302: device output-ESP32:#14#14 -> output-ESP32:#25#18
- U$303: device output-ESP32:#13#5 -> output-ESP32:#17#17
- U$304: device output-ESP32:#4#2 -> output-ESP32:#16#15
- U$305: device output-ESP32:#TX#O#0 -> output-ESP32:#14#14
- U$306: device output-ESP32:#RX#I#1 -> output-ESP32:#13#5
- U$307: device output-ESP32:#RESET#1842 -> output-ESP32:#4#2
- U$308: device output-ESP32:#BOOT#1841 -> output-ESP32:#TX#O#0
- U$309: device output-ESP32:#JTAG#1847 -> output-ESP32:#RX#I#1
- U$310: device output-ESP32:#A0#1843 -> output-ESP32:#RESET#1842
- U$311: device output-ESP32:#A3#1843 -> output-ESP32:#BOOT#1841
- U$312: device output-ESP32:#A6#1843 -> output-ESP32:#JTAG#1847
- U$313: device output-ESP32:#A7#1843 -> output-ESP32:#A0#1843
- U$314: device output-ESP32:#A4#1843 -> output-ESP32:#A3#1843
- U$315: device output-ESP32:#A5#1843 -> output-ESP32:#A6#1843
- U$316: device output-ESP32:#VIN#1843 -> output-ESP32:#A7#1843
- U$317, U$412: device output-ESP32:#GND#1844 -> output-ESP32:#A4#1843
- U$319: device output-ESP32:#5V#1845 -> output-ESP32:#VIN#1843
- U$321, U$415: device output-ESP32:##RST##1845 -> output-ESP32:#GND#1844
- U$322: device output-ESP32:#REF#1846 -> output-ESP32:#5V#1845
- U$323: device output-ESP32:#MEAS#1851 -> output-ESP32:#3#3V#1845
- U$324: device output-ESP32:#1849 -> output-ESP32:##RST##1845
- U$325: device output-ESP32:#1850 -> output-ESP32:#REF#1846
- U$326: device output-ESP32:#BATT#1848 -> output-ESP32:#MEAS#1851
- U$327: device output-ESP32:#JTAG#1847 -> output-ESP32:#1849
- U$328: device output-ESP32:ESP321855 -> output-ESP32:#1850
- U$329: device output-ESP32:7#15V32321861 -> output-ESP32:#BATT#1848
- U$330: device output-ESP32:#39#A3#321862 -> output-ESP32:#JTAG#1847
- U$331: device output-ESP32:#36#A0#321862 -> output-ESP32:ESP321855
- U$332: device output-ESP32:#34#A6#32321865 -> output-ESP32:7#15V32321861
- U$333: device output-ESP32:#35#A7#321862 -> output-ESP32:#39#A3#321862
- U$334: device output-ESP32:#32#A4#32321865 -> output-ESP32:#36#A0#321862
- U$335: device output-ESP32:#34#A6#321862 -> output-ESP32:#34#A6#32321865
- U$336: device output-ESP32:#VIN#321862 -> output-ESP32:#35#A7#321862
- U$337, U$622: device output-ESP32:#GND#321863 -> output-ESP32:#32#A4#32321865
- U$338: device output-ESP32:#5V#321864 -> output-ESP32:#34#A6#321862
- U$339: device output-ESP32:#3#3V#321864 -> output-ESP32:#VIN#321862
- U$341: device output-ESP32:##RESET##321864 -> output-ESP32:#5V#321864
- U$342: device output-ESP32:#IOREF#321865 -> output-ESP32:#3#3V#321864
- U$343, U$625: device output-ESP32:#3#RX#I#32321869 -> output-ESP32:#GND#321863
- U$344: device output-ESP32:#1#TX#O#32321869 -> output-ESP32:##RESET##321864
- U$345: device output-ESP32:#13#TCK#32321869 -> output-ESP32:#IOREF#321865
- U$346: device output-ESP32:#14#TMS#32321869 -> output-ESP32:#3#RX#I#32321869
- U$347: device output-ESP32:#16#32321869 -> output-ESP32:#1#TX#O#32321869
- U$348: device output-ESP32:#17#32321869 -> output-ESP32:#13#TCK#32321869
- U$349: device output-ESP32:#25#32321869 -> output-ESP32:#14#TMS#32321869
- U$350: device output-ESP32:#26#32321869 -> output-ESP32:#16#32321869
- U$351: device output-ESP32:#5##CS##32321869 -> output-ESP32:#17#32321869
- U$352: device output-ESP32:#23#PICO#321866 -> output-ESP32:#25#32321869
- U$353: device output-ESP32:#19#POCI#321866 -> output-ESP32:#26#32321869
- U$354: device output-ESP32:#18#SCK#32321869 -> output-ESP32:#5##CS##32321869
- U$355: device output-ESP32:#21#SDA#32321869 -> output-ESP32:#23#PICO#321866
- U$356: device output-ESP32:#22#SCL#32321869 -> output-ESP32:#19#POCI#321866
- U$357: device output-ESP32:#27#32321869 -> output-ESP32:#18#SCK#32321869
- U$358: device output-ESP32:#GND#321866 -> output-ESP32:#21#SDA#32321869
- U$359: device output-ESP32:#3#3V#321866 -> output-ESP32:#22#SCL#32321869
- U$360: device output-ESP32:#MEAS#1851 -> output-ESP32:#27#32321869
- U$361: device output-ESP32:#BYP#35 -> output-ESP32:#GND#321866
- U$362: device output-ESP32:D#32321863 -> output-ESP32:#3#3V#321866
- U$363: device output-ESP32:D#32321862 -> output-ESP32:#MEAS#1851
- U$364: device output-ESP32:G32321864 -> output-ESP32:#BYP#35
- U$365: device output-ESP32:#1849 -> output-ESP32:D#32321863
- U$366: device output-ESP32:#1850 -> output-ESP32:D#32321862
- U$367: device output-ESP32:#I2C#1855 -> output-ESP32:G32321864
- U$368: device output-ESP32:##ALERT##1852 -> output-ESP32:#1849
- U$369: device output-ESP32:#TMS#1854 -> output-ESP32:#1850
- U$370: device output-ESP32:#TCK#1853 -> output-ESP32:#I2C#1855
- U$371: device output-ESP32:MADE_IN_THE_USA321857 -> output-ESP32:##ALERT##1852
- U$372: device output-ESP32:ESP32_REDBOARD321857 -> output-ESP32:#TMS#1854
- U$373: device output-ESP32:REDBOARD321856 -> output-ESP32:#TCK#1853
- U$374, U$469: device output-ESP32:INPUT_ONLY321867 -> output-ESP32:MADE_IN_THE_USA321857
- U$376: device output-ESP32:##ALERT##4#321866 -> output-ESP32:REDBOARD321856
- U$378, U$472: device output-ESP32:#SCL#34 -> output-ESP32:INPUT_ONLY321867
- U$379: device output-ESP32:#SDA#33 -> output-ESP32:##ALERT##4#321866
- U$380: device output-ESP32:#3#3V#33 -> output-ESP32:TP1321868
- U$381: device output-ESP32:#GND#32 -> output-ESP32:V323252
- U$382: device output-ESP32:#SCK#31 -> output-ESP32:#SCL#34
- U$383: device output-ESP32:#POCI#30 -> output-ESP32:#SDA#33
- U$384: device output-ESP32:#PICO#29 -> output-ESP32:#3#3V#33
- U$385: device output-ESP32:1836 -> output-ESP32:#GND#32
- U$386: device output-ESP32:##CS##28 -> output-ESP32:#SCK#31
- U$387: device output-ESP32:#27#27 -> output-ESP32:#POCI#30
- U$388: device output-ESP32:#26#26 -> output-ESP32:#PICO#29
- U$389: device output-ESP32:TX1838 -> output-ESP32:1836
- U$390: device output-ESP32:RX1839 -> output-ESP32:##CS##28
- U$391: device output-ESP32:PWR1837 -> output-ESP32:#27#27
- U$392: device output-ESP32:CHG1840 -> output-ESP32:#26#26
- U$393: device output-ESP32:#25#18 -> output-ESP32:TX1838
- U$394: device output-ESP32:#17#17 -> output-ESP32:RX1839
- U$395: device output-ESP32:#16#15 -> output-ESP32:PWR1837
- U$396: device output-ESP32:#14#14 -> output-ESP32:CHG1840
- U$397: device output-ESP32:#13#5 -> output-ESP32:#25#18
- U$398: device output-ESP32:#4#2 -> output-ESP32:#17#17
- U$399: device output-ESP32:#TX#O#0 -> output-ESP32:#16#15
- U$400: device output-ESP32:#RX#I#1 -> output-ESP32:#14#14
- U$401: device output-ESP32:#RESET#1842 -> output-ESP32:#13#5
- U$402: device output-ESP32:#BOOT#1841 -> output-ESP32:#4#2
- U$403: device output-ESP32:#JTAG#1847 -> output-ESP32:#TX#O#0
- U$404: device output-ESP32:#A0#1843 -> output-ESP32:#RX#I#1
- U$405: device output-ESP32:#A3#1843 -> output-ESP32:#RESET#1842
- U$406: device output-ESP32:#A6#1843 -> output-ESP32:#BOOT#1841
- U$407: device output-ESP32:#A7#1843 -> output-ESP32:#JTAG#1847
- U$408: device output-ESP32:#A4#1843 -> output-ESP32:#A0#1843
- U$409: device output-ESP32:#A5#1843 -> output-ESP32:#A3#1843
- U$410: device output-ESP32:#VIN#1843 -> output-ESP32:#A6#1843
- U$411, U$506: device output-ESP32:#GND#1844 -> output-ESP32:#A7#1843
- U$413: device output-ESP32:#5V#1845 -> output-ESP32:#A5#1843
- U$414: device output-ESP32:#3#3V#1845 -> output-ESP32:#VIN#1843
- U$416, U$510: device output-ESP32:#REF#1846 -> output-ESP32:#GND#1844
- U$417: device output-ESP32:#MEAS#1851 -> output-ESP32:#5V#1845
- U$418: device output-ESP32:#1849 -> output-ESP32:#3#3V#1845
- U$419: device output-ESP32:#1850 -> output-ESP32:##RST##1845
- U$420: device output-ESP32:#BATT#1848 -> output-ESP32:#REF#1846
- U$421: device output-ESP32:#JTAG#1847 -> output-ESP32:#MEAS#1851
- U$422: device output-ESP32:ESP321855 -> output-ESP32:#1849
- U$423: device output-ESP32:7#15V32321861 -> output-ESP32:#1850
- U$424: device output-ESP32:#39#A3#321862 -> output-ESP32:#BATT#1848
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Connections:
- net ESP32_GPIO12_TDI: now also TP1.1
- net ESP32_GPIO12_TDI1: now also TP2.1
- net ESP32_GPIO12_TDI10: now also TP11.1
- net ESP32_GPIO12_TDI11: now also TP12.1
- net ESP32_GPIO12_TDI2: now also TP3.1
- net ESP32_GPIO12_TDI3: now also TP4.1
- net ESP32_GPIO12_TDI4: now also TP5.1
- net ESP32_GPIO12_TDI5: now also TP6.1
- net ESP32_GPIO12_TDI6: now also TP7.1
- net ESP32_GPIO12_TDI7: now also TP8.1
- net ESP32_GPIO12_TDI8: now also TP9.1
- net ESP32_GPIO12_TDI9: now also TP10.1
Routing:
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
